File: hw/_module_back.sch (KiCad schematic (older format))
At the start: 74 parts, among them J12 power_bus, Q2 2SC1815, Q3 2SC1815, Q4 2SC1815, Q5 2SC1815, Q6 2SC1815, Q7 2SC1815, Q8 2SC1815, Q9 2SC1815, U10 LM2950G-3.3, U7 TL074, U8 TL074, U9 TL072

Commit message: hardware: artwork done.
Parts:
- C11, C12, C13: footprint (none) -> Attenuverter:C_Axial_L4.8mm_D2.0mm_P2.54mm_Horizontal
- C14, C15: footprint (none) -> Capacitor_THT:CP_Radial_D6.3mm_P2.50mm
- C16, C17: footprint (none) -> Capacitor_THT:CP_Radial_D5.0mm_P2.50mm
- D14, D15, D16, D17, D18, D19, D20, D21: footprint Diode_THT:D_DO-35_SOD27_P7.62mm_Horizontal -> Diode_THT:D_DO-35_SOD27_P2.54mm_Vertical_AnodeUp
- J16, J17: renamed from J?; footprint (none) -> Connector_PinHeader_2.54mm:PinHeader_2x08_P2.54mm_Vertical
- J18: renamed from J12; footprint (none) -> Connector_PinHeader_2.54mm:PinHeader_2x05_P2.54mm_Vertical
- Q2, Q3, Q4, Q5, Q6, Q7, Q8, Q9, U10: footprint Package_TO_SOT_THT:TO-92_Inline -> Package_TO_SOT_THT:TO-92_Inline_Wide
- R27, R28, R29, R30, R31, R32, R33, R34, R35, R36, R37, R38, R39, R40, R41, R42, R43, R44, R45, R46, R47, R48, R49, R50, R51, R52, R53, R54, R55, R56, R57, R58, R59, R60, R61, R62, R63, R64, R65, R66, R67, R68, R69, R70: footprint (none) -> Resistor_THT:R_Axial_DIN0207_L6.3mm_D2.5mm_P2.54mm_Vertical
- U7, U8: footprint (none) -> Package_DIP:DIP-14_W7.62mm
- U9: footprint (none) -> Package_DIP:DIP-8_W7.62mm
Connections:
- net +3V3: now also J17.9 (Pin_9); no longer J17.7 (Pin_7)
- net cv1: now also J17.6 (Pin_6); no longer J17.12 (Pin_12)
- net cv2: now also J17.14 (Pin_14); no longer J17.16 (Pin_16)
- net cv_2_in: now also J17.12 (Pin_12); no longer J17.14 (Pin_14)
- net dac_1_a: now also J16.3 (Pin_3); no longer J16.2 (Pin_2)
- net dac_1_b: now also J16.5 (Pin_5); no longer J16.3 (Pin_3)
- net dac_2_a: now also J16.13 (Pin_13); no longer J16.11 (Pin_11)
- net dac_2_b: now also J16.15 (Pin_15); no longer J16.6 (Pin_6)
- net dac_3_a: now also J17.2 (Pin_2); no longer J16.14 (Pin_14)
- net dac_3_b: now also J17.1 (Pin_1); no longer J17.13 (Pin_13)
- net dac_4_a: now also J17.7 (Pin_7); no longer J17.5 (Pin_5)
- net dac_4_b: now also J17.11 (Pin_11); no longer J17.2 (Pin_2)
- net out_1: now also J16.1 (Pin_1); no longer J16.4 (Pin_4)
- net out_2: now also J16.7 (Pin_7); no longer J16.5 (Pin_5)
- net out_3: now also J16.11 (Pin_11); no longer J16.15 (Pin_15)
- net out_4: now also J16.16 (Pin_16); no longer J16.12 (Pin_12)
- net out_5: now also J17.4 (Pin_4); no longer J17.15 (Pin_15)
- net out_6: now also J17.3 (Pin_3); no longer J17.9 (Pin_9)
- net out_7: now also J17.5 (Pin_5); no longer J17.1 (Pin_1)
- net out_8: now also J17.13 (Pin_13); no longer J17.6 (Pin_6)
- net polarity_1: now also J16.2 (Pin_2); no longer J16.1 (Pin_1)
- net polarity_2: now also J16.4 (Pin_4); no longer J16.7 (Pin_7)
- net polarity_3: now also J16.12 (Pin_12); no longer J16.13 (Pin_13)
- net polarity_4: now also J16.14 (Pin_14); no longer J16.10 (Pin_10)
- net polarity_5: now also J16.6 (Pin_6); no longer J16.16 (Pin_16)
- net polarity_6: now also J16.10 (Pin_10); no longer J17.11 (Pin_11)
- net polarity_7: now also J17.16 (Pin_16); no longer J17.3 (Pin_3)
- net polarity_8: now also J17.15 (Pin_15); no longer J17.4 (Pin_4)

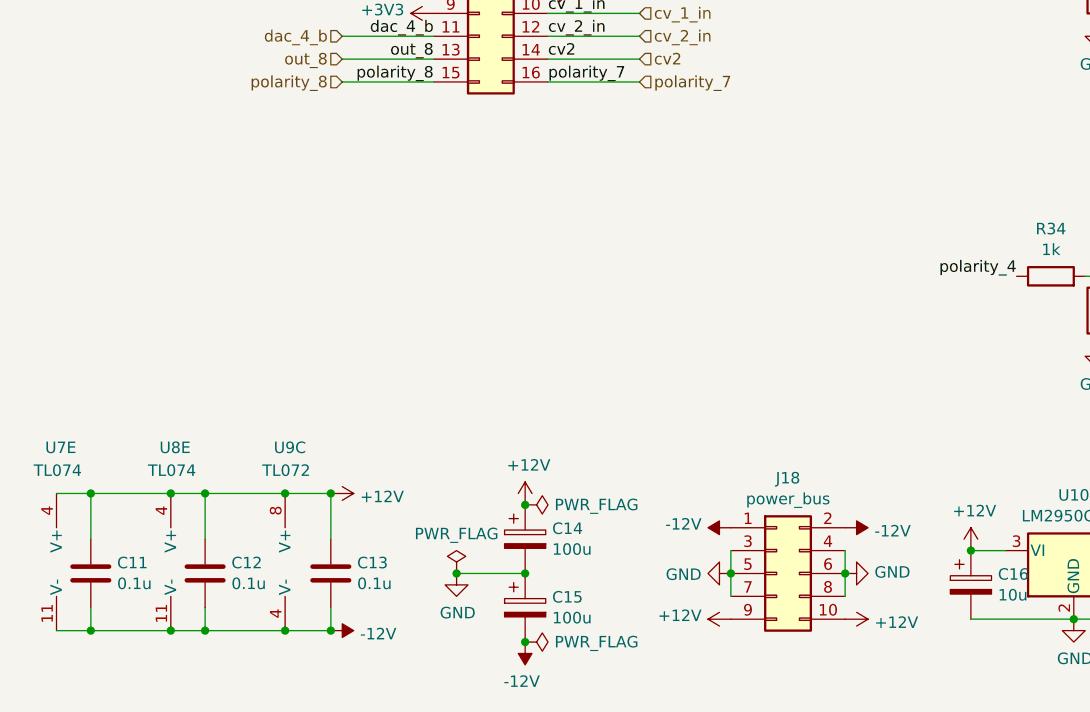
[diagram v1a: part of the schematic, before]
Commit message: Software: appended polarity selection functionality. Hardware: appended power reversal protection.           adjusted silks.
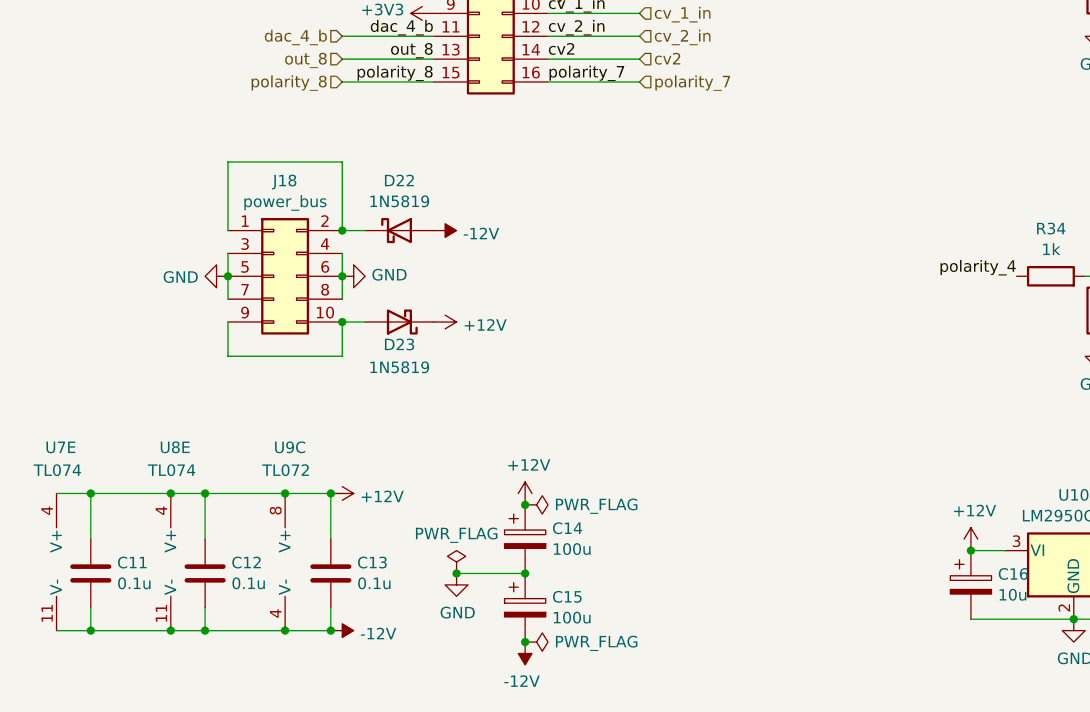
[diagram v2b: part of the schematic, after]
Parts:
- added D22, D23: 1N5819, Diode_THT:D_DO-41_SOD81_P2.54mm_Vertical_AnodeUp, symbol Diode:1N5819
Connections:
- net +12V: now also D23.1 (K); no longer J18.10 (Pin_10), J18.9 (Pin_9)
- net -12V: now also D22.2 (A); no longer J18.1 (Pin_1), J18.2 (Pin_2)
- new net: D22.1 (K), J18.1 (Pin_1), J18.2 (Pin_2)
- new net: D23.2 (A), J18.10 (Pin_10), J18.9 (Pin_9)
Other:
- moved on the sheet: J18
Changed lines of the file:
@@
 $Descr A4 11693 8268
 encoding utf-8
-Sheet 2 2
+Sheet 4 4
 Title ""
 Date ""
@@
 L Connector_Generic:Conn_02x05_Odd_Even J?
 U 1 1 63FEBBC8
-P 4100 7150
+P 1900 5850
 AR Path="/63FEBBC8" Ref="J?"  Part="1"
 AR Path="/63F3B749/63FEBBC8" Ref="J18"  Part="1"
-F 0 "J18" H 4150 7567 50  0000 C CNN
-F 1 "power_bus" H 4150 7476 50  0000 C CNN
-F 2 "Connector_PinHeader_2.54mm:PinHeader_2x05_P2.54mm_Vertical" H 4100 7150 50  0001 C CNN
-F 3 "~" H 4100 7150 50  0001 C CNN
-	1    4100 7150
-	1    0    0    -1
-$EndComp
-$Comp
-L power:+12V #PWR?
-U 1 1 63FEBBCE
-P 3900 7350
-AR Path="/63FEBBCE" Ref="#PWR?"  Part="1"
-AR Path="/63F3B749/63FEBBCE" Ref="#PWR098"  Part="1"
-F 0 "#PWR098" H 3900 7200 50  0001 C CNN
-F 1 "+12V" V 3915 7478 50  0000 L CNN
-F 2 "" H 3900 7350 50  0001 C CNN
-F 3 "" H 3900 7350 50  0001 C CNN
-	1    3900 7350
-	0    -1   -1   0
+F 0 "J18" H 1950 6267 50  0000 C CNN
+F 1 "power_bus" H 1950 6176 50  0000 C CNN
+F 2 "Connector_PinHeader_2.54mm:PinHeader_2x05_P2.54mm_Vertical" H 1900 5850 50  0001 C CNN
+F 3 "~" H 1900 5850 50  0001 C CNN
+	1    1900 5850
+	1    0    0    -1
 $EndComp
 $Comp
 L power:+12V #PWR?
 U 1 1 63FEBBD4
-P 4400 7350
+P 2600 6050
 AR Path="/63FEBBD4" Ref="#PWR?"  Part="1"
 AR Path="/63F3B749/63FEBBD4" Ref="#PWR0101"  Part="1"
-F 0 "#PWR0101" H 4400 7200 50  0001 C CNN
-F 1 "+12V" V 4415 7478 50  0000 L CNN
-F 2 "" H 4400 7350 50  0001 C CNN
-F 3 "" H 4400 7350 50  0001 C CNN
-	1    4400 7350
+F 0 "#PWR0101" H 2600 5900 50  0001 C CNN
+F 1 "+12V" V 2615 6178 50  0000 L CNN
+F 2 "" H 2600 6050 50  0001 C CNN
+F 3 "" H 2600 6050 50  0001 C CNN
+	1    2600 6050
 	0    1    1    0
-$EndComp
-$Comp
-L power:-12V #PWR?
-U 1 1 63FEBBDA
-P 3900 6950
-AR Path="/63FEBBDA" Ref="#PWR?"  Part="1"
-AR Path="/63F3B749/63FEBBDA" Ref="#PWR096"  Part="1"
-F 0 "#PWR096" H 3900 7050 50  0001 C CNN
-F 1 "-12V" V 3915 7078 50  0000 L CNN
-F 2 "" H 3900 6950 50  0001 C CNN
-F 3 "" H 3900 6950 50  0001 C CNN
-	1    3900 6950
-	0    -1   -1   0
 $EndComp
 $Comp
 L power:-12V #PWR?
 U 1 1 63FEBBE0
-P 4400 6950
+P 2600 5650
 AR Path="/63FEBBE0" Ref="#PWR?"  Part="1"
 AR Path="/63F3B749/63FEBBE0" Ref="#PWR099"  Part="1"
-F 0 "#PWR099" H 4400 7050 50  0001 C CNN
-F 1 "-12V" V 4415 7078 50  0000 L CNN
-F 2 "" H 4400 6950 50  0001 C CNN
-F 3 "" H 4400 6950 50  0001 C CNN
-	1    4400 6950
+F 0 "#PWR099" H 2600 5750 50  0001 C CNN
+F 1 "-12V" V 2615 5778 50  0000 L CNN
+F 2 "" H 2600 5650 50  0001 C CNN
+F 3 "" H 2600 5650 50  0001 C CNN
+	1    2600 5650
 	0    1    1    0
 $EndComp
@@
 L power:GND #PWR?
 U 1 1 63FEBBE6
-P 3900 7150
+P 1700 5850
 AR Path="/63FEBBE6" Ref="#PWR?"  Part="1"
 AR Path="/63F3B749/63FEBBE6" Ref="#PWR097"  Part="1"
-F 0 "#PWR097" H 3900 6900 50  0001 C CNN
-F 1 "GND" V 3905 7022 50  0000 R CNN
-F 2 "" H 3900 7150 50  0001 C CNN
-F 3 "" H 3900 7150 50  0001 C CNN
-	1    3900 7150
+F 0 "#PWR097" H 1700 5600 50  0001 C CNN
+F 1 "GND" V 1705 5722 50  0000 R CNN
+F 2 "" H 1700 5850 50  0001 C CNN
+F 3 "" H 1700 5850 50  0001 C CNN
+	1    1700 5850
 	0    1    1    0
 $EndComp
@@
 L power:GND #PWR?
 U 1 1 63FEBBEC
-P 4400 7150
+P 2200 5850
 AR Path="/63FEBBEC" Ref="#PWR?"  Part="1"
 AR Path="/63F3B749/63FEBBEC" Ref="#PWR0100"  Part="1"
-F 0 "#PWR0100" H 4400 6900 50  0001 C CNN
-F 1 "GND" V 4405 7022 50  0000 R CNN
-F 2 "" H 4400 7150 50  0001 C CNN
-F 3 "" H 4400 7150 50  0001 C CNN
-	1    4400 7150
+F 0 "#PWR0100" H 2200 5600 50  0001 C CNN
+F 1 "GND" V 2205 5722 50  0000 R CNN
+F 2 "" H 2200 5850 50  0001 C CNN
+F 3 "" H 2200 5850 50  0001 C CNN
+	1    2200 5850
 	0    -1   -1   0
 $EndComp
 Wire Wire Line
-	3900 7050 3900 7150
-Connection ~ 3900 7150
-Wire Wire Line
-	3900 7150 3900 7250
-Wire Wire Line
-	4400 7050 4400 7150
-Connection ~ 4400 7150
-Wire Wire Line
-	4400 7150 4400 7250
+	1700 5750 1700 5850
+Connection ~ 1700 5850
+Wire Wire Line
+	1700 5850 1700 5950
+Wire Wire Line
+	2200 5750 2200 5850
+Connection ~ 2200 5850
+Wire Wire Line
+	2200 5850 2200 5950
 $Comp
 L Regulator_Linear:LM78L05_TO92 U?
@@
 Wire Wire Line
 	2600 4300 2200 4300
+$Comp
+L Diode:1N5819 D22
+U 1 1 62AEFE36
+P 2450 5650
+F 0 "D22" H 2450 5867 50  0000 C CNN
+F 1 "1N5819" H 2450 5776 50  0000 C CNN
+F 2 "Diode_THT:D_DO-41_SOD81_P2.54mm_Vertical_AnodeUp" H 2450 5475 50  0001 C CNN
+F 3 "http://www.vishay.com/docs/88525/1n5817.pdf" H 2450 5650 50  0001 C CNN
+	1    2450 5650
+	1    0    0    -1
+$EndComp
+Wire Wire Line
+	1700 5650 1700 5350
+Wire Wire Line
+	1700 5350 2200 5350
+Wire Wire Line
+	2200 5350 2200 5650
+Wire Wire Line
+	2200 5650 2300 5650
+Connection ~ 2200 5650
+$Comp
+L Diode:1N5819 D23
+U 1 1 62B168FF
+P 2450 6050
+F 0 "D23" H 2450 6150 50  0000 C CNN
+F 1 "1N5819" H 2450 6250 50  0000 C CNN
+F 2 "Diode_THT:D_DO-41_SOD81_P2.54mm_Vertical_AnodeUp" H 2450 5875 50  0001 C CNN
+F 3 "http://www.vishay.com/docs/88525/1n5817.pdf" H 2450 6050 50  0001 C CNN
+	1    2450 6050
+	-1   0    0    1
+$EndComp
+Wire Wire Line
+	1700 6050 1700 6200
+Wire Wire Line
+	1700 6200 2200 6200
+Wire Wire Line
+	2200 6200 2200 6050
+Wire Wire Line
+	2200 6050 2300 6050
+Connection ~ 2200 6050
 $EndSCHEMATC

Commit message: Software: - Added CV control, but for limited functions. - Added BPM mode.
Hardware:
- Version ordered to Elecrow.
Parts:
- added D16: BAT48JFILM, Diode_THT:D_DO-35_SOD27_P7.62mm_Horizontal, symbol Diode:BAT48JFILM
- renumbered D22 to D14, D23 to D15, D14 to D17, D15 to D18, D16 to D19, D17 to D20, D18 to D21, D19 to D22, D20 to D23, D21 to D24, J18 to J17, J17 to J18
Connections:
- net +12V: now also D16.1 (K)
- net +3V3: now also D16.2 (A)
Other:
- moved on the sheet: C16, C17, U10
